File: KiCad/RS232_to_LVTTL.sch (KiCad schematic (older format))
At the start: 1 part, among them J1 DB25_Female

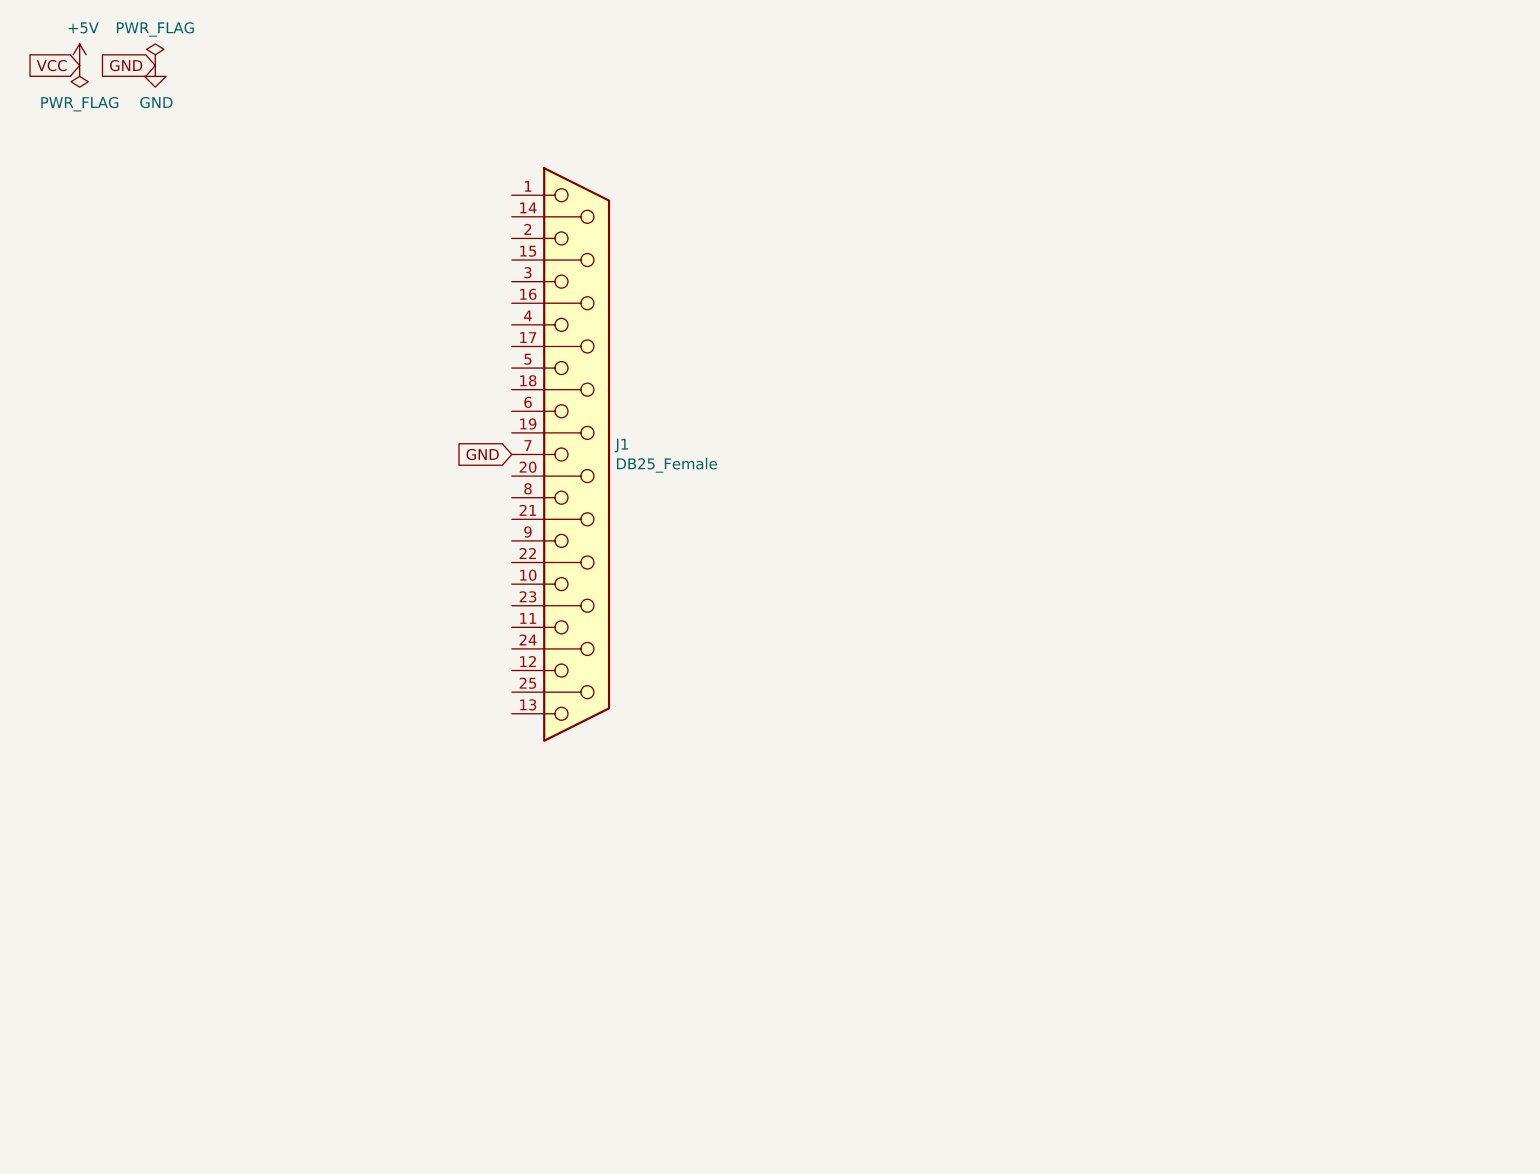
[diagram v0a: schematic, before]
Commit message: Added power circuit convert 12V to 3.3V
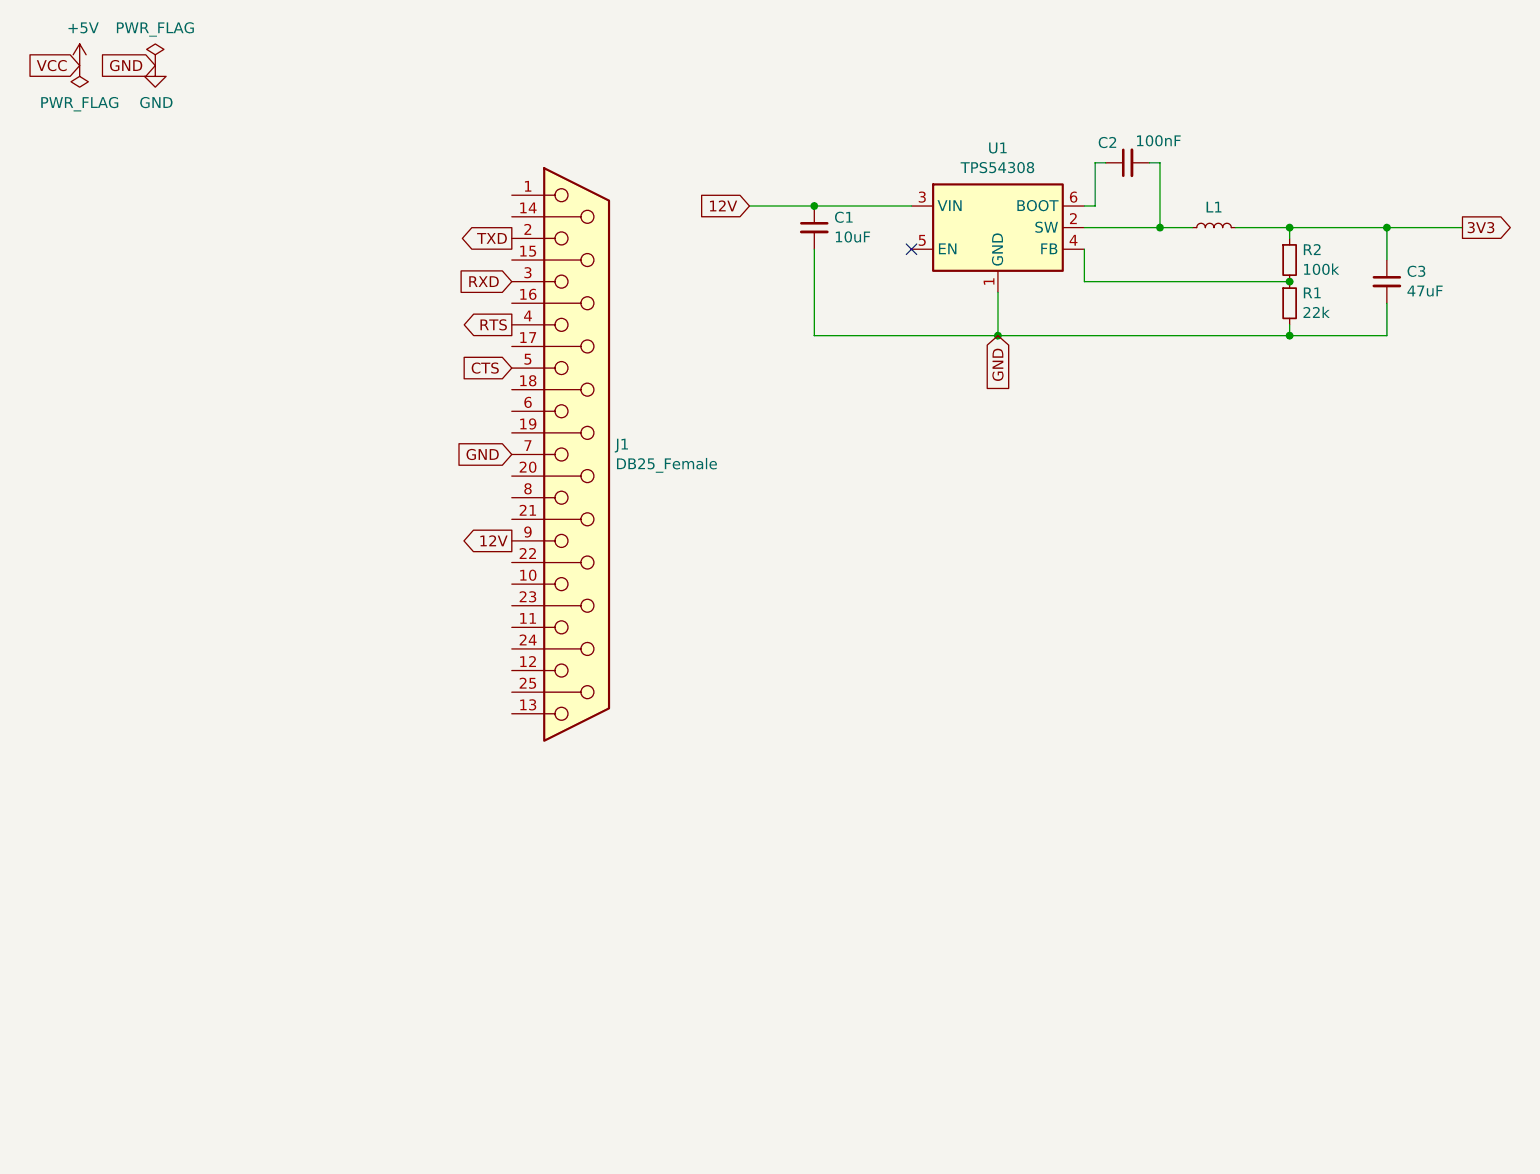
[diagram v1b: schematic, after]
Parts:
- added C1: 10uF, Capacitor_SMD:C_0805_2012Metric_Pad1.15x1.40mm_HandSolder, symbol Device:C_Small
- added C2: 100nF, Capacitor_SMD:C_0805_2012Metric_Pad1.15x1.40mm_HandSolder, symbol Device:C_Small
- added C3: 47uF, Capacitor_SMD:C_1206_3216Metric_Pad1.42x1.75mm_HandSolder, symbol Device:C_Small
- added L1: L_Small, Inductor_SMD:L_Wuerth_HCM-7050, symbol Device:L_Small
- added R1: 22k, Resistor_SMD:R_0603_1608Metric_Pad1.05x0.95mm_HandSolder, symbol Device:R_Small
- added R2: 100k, Resistor_SMD:R_0603_1608Metric_Pad1.05x0.95mm_HandSolder, symbol Device:R_Small
- added U1: TPS54308, Package_TO_SOT_SMD:SOT-23-6, symbol Regulator_Switching:TPS54308
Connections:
- net GND: now also C1.2, C3.2, R1.2, U1.1 (GND)
- net TXD: now reaches J1.2
- net RXD: now reaches J1.3
- net RTS: now reaches J1.4
- net CTS: now reaches J1.5
- net 12V: now reaches J1.9
- net 12V: now also C1.1, U1.3 (VIN)
- new net: C2.2, L1.1, U1.2 (SW)
- new net: R1.1, R2.2, U1.4 (FB)
- new net: C2.1, U1.6 (BOOT)
- new net 3V3: C3.1, L1.2, R2.1
- no-connect marks 0 -> 1
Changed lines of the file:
@@
 Text GLabel 2950 2750 0    50   Input ~ 0
 GND
+$Comp
+L Regulator_Switching:TPS54308 U1
+U 1 1 64259E9C
+P 5200 1700
+F 0 "U1" H 5200 2067 50  0000 C CNN
+F 1 "TPS54308" H 5200 1976 50  0000 C CNN
+F 2 "Package_TO_SOT_SMD:SOT-23-6" H 5250 1350 50  0001 L CNN
+F 3 "http://www.ti.com/lit/ds/symlink/tps54308.pdf" H 4900 2050 50  0001 C CNN
+	1    5200 1700
+	1    0    0    -1
+$EndComp
+Text GLabel 2950 3150 0    50   Output ~ 0
+12V
+Text GLabel 4050 1600 0    50   Input ~ 0
+12V
+Text GLabel 5200 2200 3    50   Input ~ 0
+GND
+NoConn ~ 4800 1800
+$Comp
+L Device:C_Small C1
+U 1 1 6425EF30
+P 4350 1700
+F 0 "C1" H 4442 1746 50  0000 L CNN
+F 1 "10uF" H 4442 1655 50  0000 L CNN
+F 2 "Capacitor_SMD:C_0805_2012Metric_Pad1.15x1.40mm_HandSolder" H 4350 1700 50  0001 C CNN
+F 3 "~" H 4350 1700 50  0001 C CNN
+	1    4350 1700
+	1    0    0    -1
+$EndComp
+Wire Wire Line
+	4050 1600 4350 1600
+Connection ~ 4350 1600
+Wire Wire Line
+	4350 1600 4800 1600
+Wire Wire Line
+	4350 1800 4350 2200
+Wire Wire Line
+	4350 2200 5200 2200
+Wire Wire Line
+	5200 2000 5200 2200
+$Comp
+L Device:R_Small R1
+U 1 1 64266682
+P 6550 2050
+F 0 "R1" H 6609 2096 50  0000 L CNN
+F 1 "22k" H 6609 2005 50  0000 L CNN
+F 2 "Resistor_SMD:R_0603_1608Metric_Pad1.05x0.95mm_HandSolder" H 6550 2050 50  0001 C CNN
+F 3 "~" H 6550 2050 50  0001 C CNN
+	1    6550 2050
+	1    0    0    -1
+$EndComp
+$Comp
+L Device:R_Small R2
+U 1 1 64268408
+P 6550 1850
+F 0 "R2" H 6609 1896 50  0000 L CNN
+F 1 "100k" H 6609 1805 50  0000 L CNN
+F 2 "Resistor_SMD:R_0603_1608Metric_Pad1.05x0.95mm_HandSolder" H 6550 1850 50  0001 C CNN
+F 3 "~" H 6550 1850 50  0001 C CNN
+	1    6550 1850
+	1    0    0    -1
+$EndComp
+Wire Wire Line
+	5600 1700 5950 1700
+$Comp
+L Device:C_Small C2
+U 1 1 6426B6A1
+P 5800 1400
+F 0 "C2" V 5892 1446 50  0000 L CNN
+F 1 "100nF" V 5900 1150 50  0000 L CNN
+F 2 "Capacitor_SMD:C_0805_2012Metric_Pad1.15x1.40mm_HandSolder" H 5800 1400 50  0001 C CNN
+F 3 "~" H 5800 1400 50  0001 C CNN
+	1    5800 1400
+	0    -1   -1   0
+$EndComp
+Wire Wire Line
+	5600 1600 5650 1600
+Wire Wire Line
+	5650 1600 5650 1400
+Wire Wire Line
+	5650 1400 5700 1400
+Wire Wire Line
+	5900 1400 5950 1400
+Wire Wire Line
+	5950 1400 5950 1700
+Text GLabel 2950 1750 0    50   Output ~ 0
+TXD
+Text GLabel 2950 1950 0    50   Input ~ 0
+RXD
+Text GLabel 2950 2150 0    50   Output ~ 0
+RTS
+Text GLabel 2950 2350 0    50   Input ~ 0
+CTS
+$Comp
+L Device:L_Small L1
+U 1 1 64272939
+P 6200 1700
+F 0 "L1" V 6293 1700 50  0000 C CNN
+F 1 "L_Small" H 6248 1655 50  0001 L CNN
+F 2 "Inductor_SMD:L_Wuerth_HCM-7050" H 6200 1700 50  0001 C CNN
+F 3 "~" H 6200 1700 50  0001 C CNN
+	1    6200 1700
+	0    -1   -1   0
+$EndComp
+Wire Wire Line
+	5950 1700 6100 1700
+Connection ~ 5950 1700
+Wire Wire Line
+	6300 1700 6550 1700
+Wire Wire Line
+	5600 1800 5600 1950
+Wire Wire Line
+	5200 2200 6550 2200
+Connection ~ 5200 2200
+Wire Wire Line
+	6550 1750 6550 1700
+Wire Wire Line
+	6550 2200 6550 2150
+Wire Wire Line
+	6550 1950 5600 1950
+Connection ~ 6550 1950
+$Comp
+L Device:C_Small C3
+U 1 1 6427A17F
+P 7000 1950
+F 0 "C3" H 7092 1996 50  0000 L CNN
+F 1 "47uF" H 7092 1905 50  0000 L CNN
+F 2 "Capacitor_SMD:C_1206_3216Metric_Pad1.42x1.75mm_HandSolder" H 7000 1950 50  0001 C CNN
+F 3 "~" H 7000 1950 50  0001 C CNN
+	1    7000 1950
+	1    0    0    -1
+$EndComp
+Wire Wire Line
+	6550 1700 7000 1700
+Wire Wire Line
+	7000 1700 7000 1850
+Connection ~ 6550 1700
+Wire Wire Line
+	6550 2200 7000 2200
+Wire Wire Line
+	7000 2200 7000 2050
+Connection ~ 6550 2200
+Text GLabel 7350 1700 2    50   Output ~ 0
+3V3
+Wire Wire Line
+	7000 1700 7350 1700
+Connection ~ 7000 1700
 $EndSCHEMATC

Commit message: Added MAX3232 chip
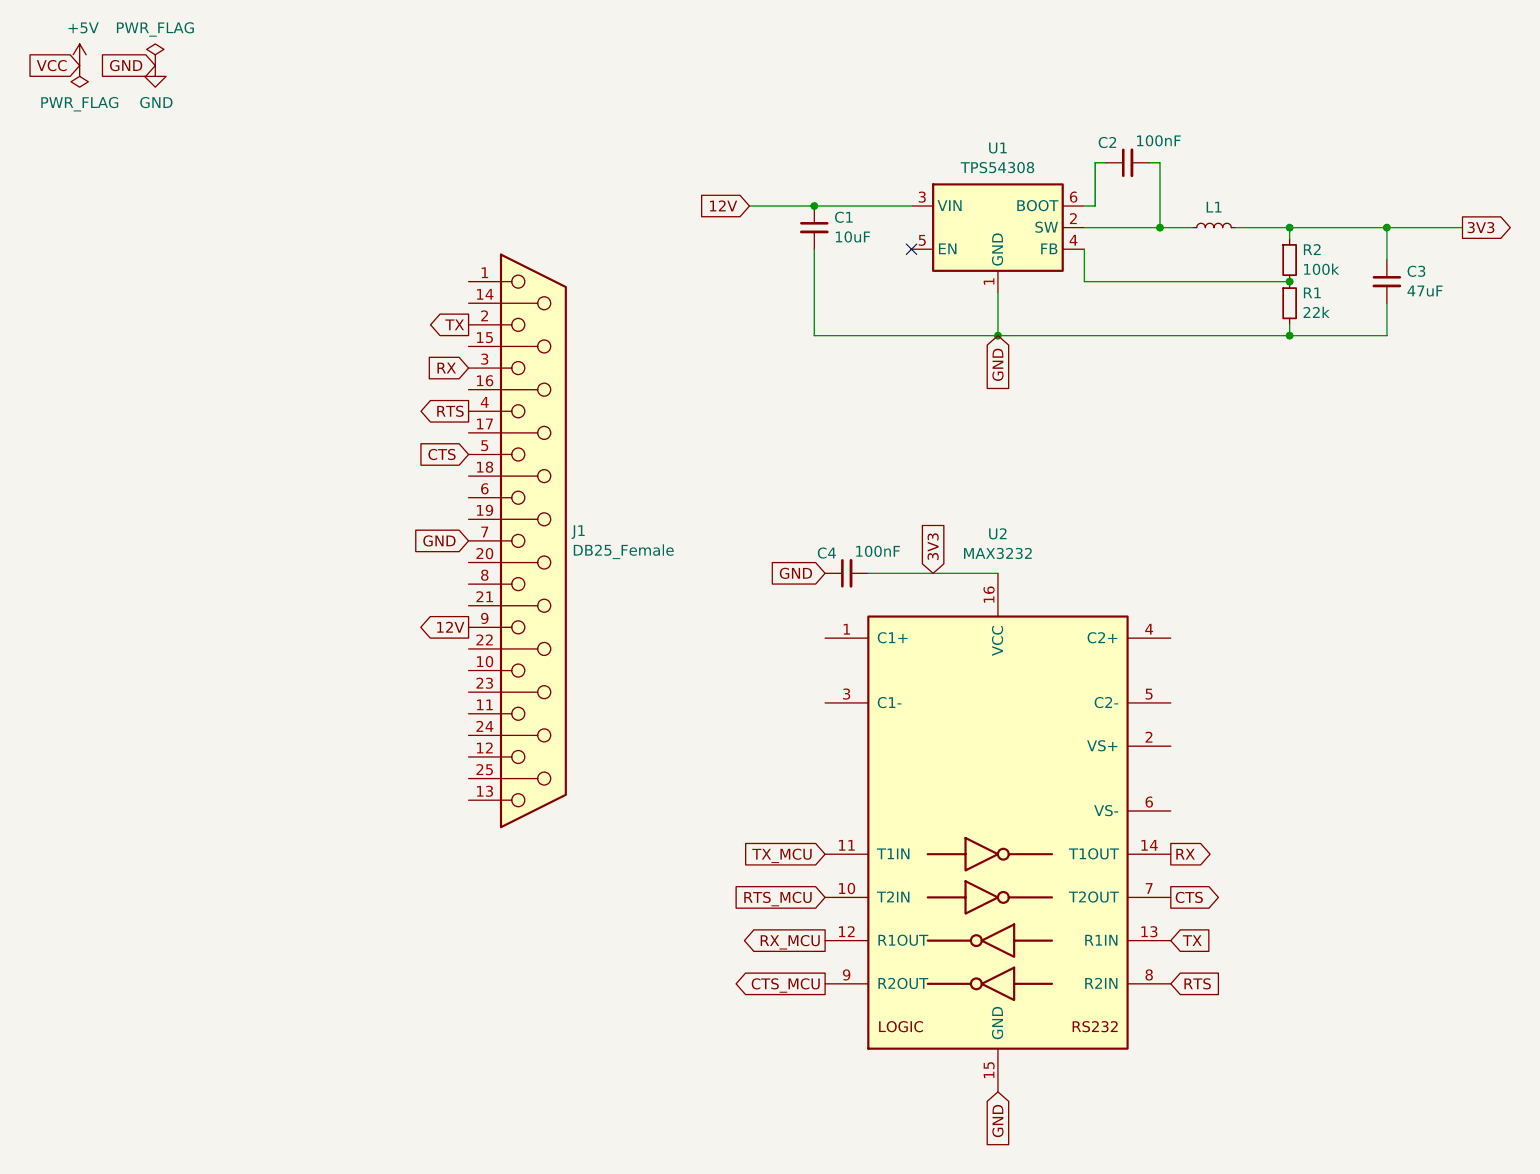
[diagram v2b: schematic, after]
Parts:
- added C4: 100nF, Capacitor_SMD:C_0805_2012Metric_Pad1.15x1.40mm_HandSolder, symbol Device:C_Small
- added U2: MAX3232, Package_SO:TSSOP-16_4.4x5mm_P0.65mm, symbol Interface_UART:MAX3232
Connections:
- net 3V3: now also C4.2, U2.16 (VCC)
- net CTS: now also U2.7 (T2OUT)
- net GND: now also C4.1, U2.15 (GND)
- net RTS: now also U2.8 (R2IN)
- net RXD renamed RX
- net RX: now also U2.14 (T1OUT)
- net TXD renamed TX
- net TX: now also U2.13 (R1IN)
- new net CTS_MCU: U2.9 (R2OUT)
- new net RTS_MCU: U2.10 (T2IN)
- new net RX_MCU: U2.12 (R1OUT)
- new net TX_MCU: U2.11 (T1IN)
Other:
- moved on the sheet: J1
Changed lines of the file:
@@
 L Connector:DB25_Female J1
 U 1 1 6426BBDB
-P 3250 2750
-F 0 "J1" H 3430 2796 50  0000 L CNN
-F 1 "DB25_Female" H 3430 2705 50  0000 L CNN
-F 2 "Connector_Dsub:DSUB-25_Female_EdgeMount_P2.77mm" H 3250 2750 50  0001 C CNN
-F 3 " ~" H 3250 2750 50  0001 C CNN
-	1    3250 2750
-	1    0    0    -1
-$EndComp
-Text GLabel 2950 2750 0    50   Input ~ 0
+P 3050 3150
+F 0 "J1" H 3230 3196 50  0000 L CNN
+F 1 "DB25_Female" H 3230 3105 50  0000 L CNN
+F 2 "Connector_Dsub:DSUB-25_Female_EdgeMount_P2.77mm" H 3050 3150 50  0001 C CNN
+F 3 " ~" H 3050 3150 50  0001 C CNN
+	1    3050 3150
+	1    0    0    -1
+$EndComp
+Text GLabel 2750 3150 0    50   Input ~ 0
 GND
 $Comp
@@
 	1    0    0    -1
 $EndComp
-Text GLabel 2950 3150 0    50   Output ~ 0
+Text GLabel 2750 3550 0    50   Output ~ 0
 12V
 Text GLabel 4050 1600 0    50   Input ~ 0
@@
 Wire Wire Line
 	5950 1400 5950 1700
-Text GLabel 2950 1750 0    50   Output ~ 0
-TXD
-Text GLabel 2950 1950 0    50   Input ~ 0
-RXD
-Text GLabel 2950 2150 0    50   Output ~ 0
+Text GLabel 2750 2150 0    50   Output ~ 0
+TX
+Text GLabel 2750 2350 0    50   Input ~ 0
+RX
+Text GLabel 2750 2550 0    50   Output ~ 0
 RTS
-Text GLabel 2950 2350 0    50   Input ~ 0
+Text GLabel 2750 2750 0    50   Input ~ 0
 CTS
 $Comp
@@
 	7000 1700 7350 1700
 Connection ~ 7000 1700
+$Comp
+L Interface_UART:MAX3232 U2
+U 1 1 64282C45
+P 5200 4500
+F 0 "U2" H 5200 5881 50  0000 C CNN
+F 1 "MAX3232" H 5200 5790 50  0000 C CNN
+F 2 "Package_SO:TSSOP-16_4.4x5mm_P0.65mm" H 5250 3450 50  0001 L CNN
+F 3 "https://datasheets.maximintegrated.com/en/ds/MAX3222-MAX3241.pdf" H 5200 4600 50  0001 C CNN
+	1    5200 4500
+	1    0    0    -1
+$EndComp
+$Comp
+L Device:C_Small C4
+U 1 1 6428B97E
+P 4500 3300
+F 0 "C4" V 4592 3346 50  0000 L CNN
+F 1 "100nF" V 4600 3050 50  0000 L CNN
+F 2 "Capacitor_SMD:C_0805_2012Metric_Pad1.15x1.40mm_HandSolder" H 4500 3300 50  0001 C CNN
+F 3 "~" H 4500 3300 50  0001 C CNN
+	1    4500 3300
+	0    -1   -1   0
+$EndComp
+Text GLabel 4900 3300 1    50   Input ~ 0
+3V3
+Wire Wire Line
+	4600 3300 5200 3300
+Text GLabel 4400 3300 0    50   Input ~ 0
+GND
+Text GLabel 6000 4600 2    50   Output ~ 0
+RX
+Text GLabel 6000 5000 2    50   Input ~ 0
+TX
+Text GLabel 6000 5200 2    50   Input ~ 0
+RTS
+Text GLabel 6000 4800 2    50   Output ~ 0
+CTS
+Text GLabel 4400 4600 0    50   Input ~ 0
+TX_MCU
+Text GLabel 4400 5000 0    50   Output ~ 0
+RX_MCU
+Text GLabel 4400 4800 0    50   Input ~ 0
+RTS_MCU
+Text GLabel 4400 5200 0    50   Output ~ 0
+CTS_MCU
+Text GLabel 5200 5700 3    50   Input ~ 0
+GND
 $EndSCHEMATC

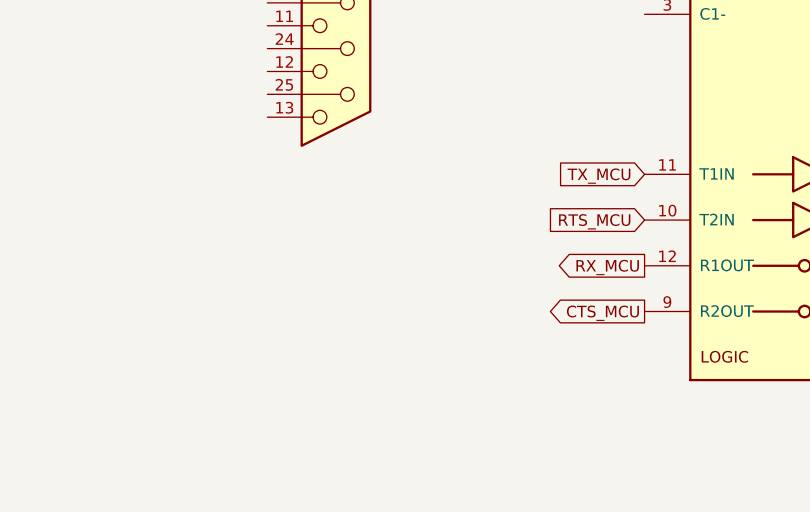
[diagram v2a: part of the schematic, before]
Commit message: Added 5-pin header for TX,RX,RTS,CTS,GND
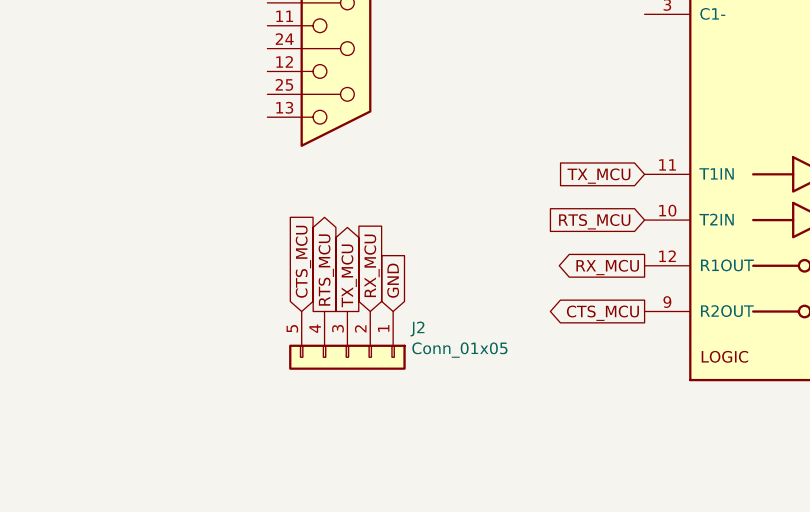
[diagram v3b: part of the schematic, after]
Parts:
- added J2: Conn_01x05, Connector_PinHeader_2.54mm:PinHeader_1x05_P2.54mm_Vertical, symbol Connector_Generic:Conn_01x05
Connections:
- net CTS_MCU: now also J2.5 (Pin_5)
- net GND: now also J2.1 (Pin_1)
- net RTS_MCU: now also J2.4 (Pin_4)
- net RX_MCU: now also J2.2 (Pin_2)
- net TX_MCU: now also J2.3 (Pin_3)
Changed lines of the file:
@@
 Text GLabel 5200 5700 3    50   Input ~ 0
 GND
+$Comp
+L Connector_Generic:Conn_01x05 J2
+U 1 1 6429DBB7
+P 3100 5400
+F 0 "J2" V 2972 5680 50  0000 L CNN
+F 1 "Conn_01x05" V 3063 5680 50  0000 L CNN
+F 2 "Connector_PinHeader_2.54mm:PinHeader_1x05_P2.54mm_Vertical" H 3100 5400 50  0001 C CNN
+F 3 "~" H 3100 5400 50  0001 C CNN
+	1    3100 5400
+	0    1    1    0
+$EndComp
+Text GLabel 2900 5200 1    50   Input ~ 0
+CTS_MCU
+Text GLabel 3000 5200 1    50   Output ~ 0
+RTS_MCU
+Text GLabel 3100 5200 1    50   Output ~ 0
+TX_MCU
+Text GLabel 3200 5200 1    50   Input ~ 0
+RX_MCU
+Text GLabel 3300 5200 1    50   Input ~ 0
+GND
 $EndSCHEMATC
